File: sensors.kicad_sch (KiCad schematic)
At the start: 15 parts, among them U21 BMI088 6-axis IMU, U22 BMP581 barometer, U23 ADXL375 high-g accelerometer

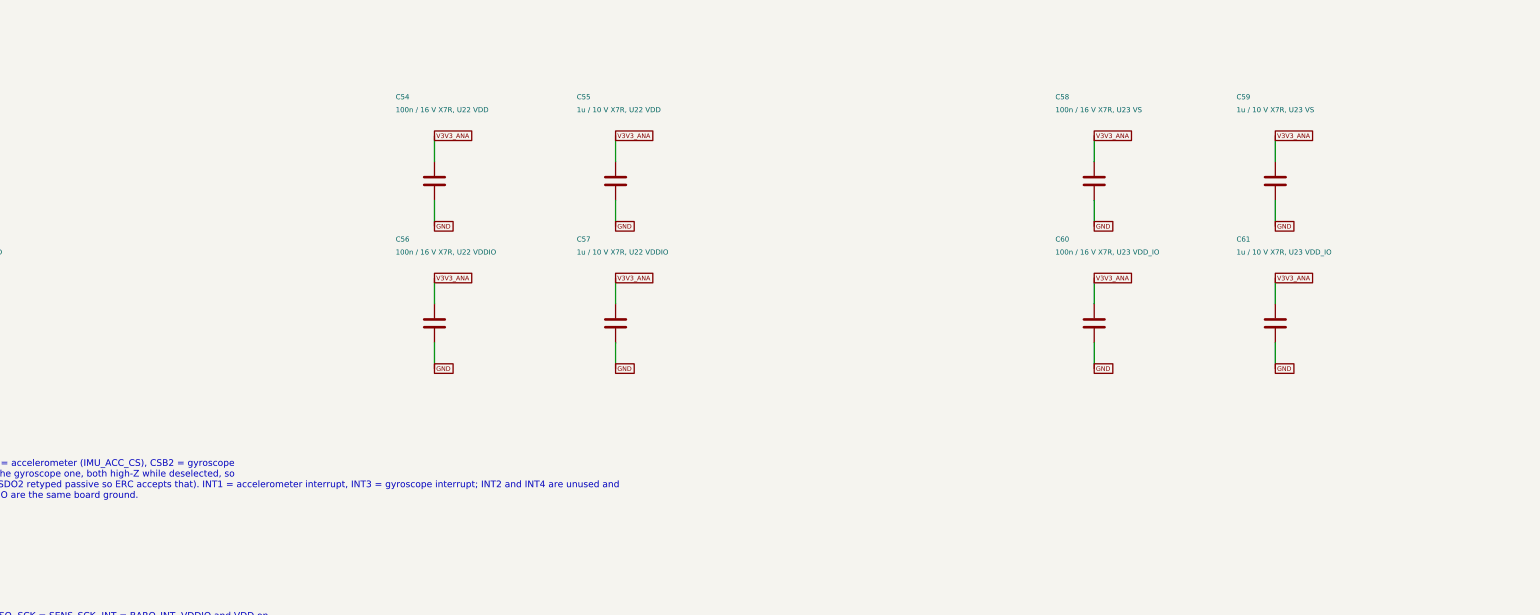
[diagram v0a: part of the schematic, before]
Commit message: Schematic review: TPS2121 input stage, DS-009 ports, sequencing and CS fixes; docs trimmed
Datasheet-grounded review of the full flight-controller schematic. Downstream
of the input everything verified pin-by-pin (TPS62913, TPS7A20, RP2354B,
BMI088/BMP581/ADXL375, W25Q128, microSD, PWM). The 5 V input stage did not:

- LM66100 (5.5 V rec-op / 6 V abs-max) replaced by one TPS2121 mux (U25):
  BEC priority on IN1, OV lockout ~5.86 V, current limit ~1.5 A, reverse
  blocking on both inputs, source status on GPIO39. Input spec 4.75-5.5 V.
- 5V_IN: 2x4.7 uF + 100 uF + SMAJ5.0A TVS; J3 JST-XH -> XT30PW-M (pin 1 GND).
- J6/J7/J9 reordered to Pixhawk DS-009 (VCC/sig/sig/GND); GPS/ELRS VCC 5 V.
- VIN_SENSE 22k/10k (full scale 10.6 V, was saturating at 5.5 V).
- TPS7A20 EN <- PWR_GOOD so V3V3_ANA rises after V3V3_SYS.
- RP2354B VREG_AVDD moved to V3V3_SYS (datasheet 6.1.8: must power up with
  VREG_VIN); ADC_AVDD stays on V3V3_ANA.
- 10k pull-ups on the four sensor chip-selects.
- ERC "global label appears once" re-enabled (0 hits).

Generator, netlist checker and SPICE decks updated (TPS2121 behavioral model,
new over-voltage and 2S mis-plug corners). Build idempotent, 143 pin mappings
PASS, ERC 0/0, all corners PASS.

Docs: POWER_*.md history removed, rationale folded into DESIGN_SPEC Decisions;
808 -> 290 lines across README, DESIGN_SPEC, LIBRARIES, simulations/README.

Co-Authored-By: Claude Fable 5.1 <noreply@anthropic.com>
Claude-Session: https://claude.ai/code/session_015cFNiWgf35VN2T43HaK8PE
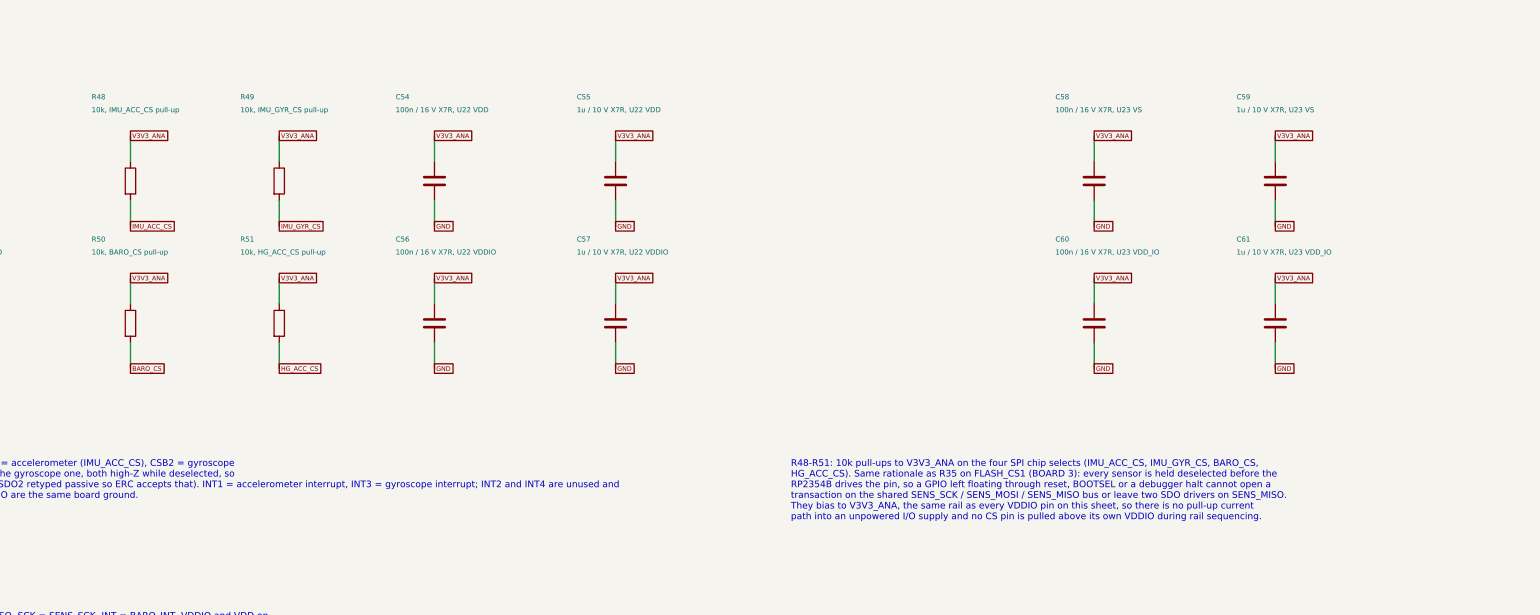
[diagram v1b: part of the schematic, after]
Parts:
- added R48: 10k, IMU_ACC_CS pull-up, Resistor_SMD:R_0603_1608Metric, symbol Device:R
- added R49: 10k, IMU_GYR_CS pull-up, Resistor_SMD:R_0603_1608Metric, symbol Device:R
- added R50: 10k, BARO_CS pull-up, Resistor_SMD:R_0603_1608Metric, symbol Device:R
- added R51: 10k, HG_ACC_CS pull-up, Resistor_SMD:R_0603_1608Metric, symbol Device:R
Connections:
- net BARO_CS: now also R50.2
- net HG_ACC_CS: now also R51.2
- net IMU_ACC_CS: now also R48.2
- net IMU_GYR_CS: now also R49.2
- net V3V3_ANA: now also R48.1, R49.1, R50.1, R51.1
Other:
- note added: "R48-R51: 10k pull-ups to V3V3_ANA on the four SPI chip selects (IMU_ACC_CS, IMU_GYR_CS, BARO_CS, HG_ACC_CS). Same rationale as R35 on FLASH_CS1 (BOARD 3): every sensor is held deselected before the RP2354B drives the pin, so a GPIO left floating through reset, BOOTSEL or a debugger halt cannot open a transaction on the shared SENS_SCK / SENS_MOSI / SENS_MISO bus or leave two SDO drivers on SENS_M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"

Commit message: Replace BMI088 with ICM-45686; vendor all footprints and 3D models for layout
Sensors: U21 is now the TDK ICM-45686 (single AP_CS on GPIO20 as IMU_CS,
INT1/INT2 on GPIO23/24, GPIO21 spare, R49 dropped, VDD+VDDIO on V3V3_ANA
with 100 nF + 1 uF each). Project-local symbol, footprint and stand-in STEP;
footprint numbering verified against DS-000577 Rev 1.0 Sec 11.2 (CCW, top
view). BMI088_SPI derived-symbol machinery removed from the generator.

Layout readiness: new tools/audit_footprints.py checks every component for
a resolvable footprint and present 3D model (128/128 OK). The seven official
KiCad footprints whose STEP files are absent from kicad-packages3d 10.0.6
are vendored into MARV_Packages.pretty with project-local models in
MARV_Packages.3dshapes: manufacturer STEPs (Coilcraft XGL4030, Molex
104031-0811), EasyEDA model (HRO TYPE-C-31-M-12), FreeCAD-generated bodies
from tools/3d/ (RP2354B QFN-80, TPS62913 RPU0010A, TPS2121 RUX0012A, Amass
XT30PW-M), and KiCad generic stand-ins (BMP581, ADXL375). Model offsets were
derived by measurement and confirmed in a rendered check board.
PROVENANCE.md records source, licence and SHA256 per model; LIBRARIES.md
lists the pre-fab 3D-viewer checks and the unverified dimensions.

Checks: build idempotent, ERC 0/0, check_power_netlist 149 mappings /
128 components, run_power_checks PASS, audit 0 needing action.

Co-Authored-By: Claude Fable 5.1 <noreply@anthropic.com>
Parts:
- removed R49: 10k, IMU_GYR_CS pull-up, Resistor_SMD:R_0603_1608Metric, symbol Device:R
- R48: value 10k, IMU_ACC_CS pull-up -> 10k, IMU_CS pull-up
- U21: value BMI088 6-axis IMU -> ICM-45686 6-axis IMU; footprint Package_LGA:Bosch_LGA-16_4.5x3mm_P0.5mm_LayoutBorder7x1y_ClockwisePinNumbering -> MARV_Packages:InvenSense_LGA-14_2.5x3mm_P0.5mm_ICM45686; symbol MARV_Power:BMI088_SPI -> MARV_Sensors:ICM-45686
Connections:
- net IMU_GYR_CS is gone; now on net V3V3_ANA: U21.5 (VDDIO)
- net IMU_GYR_INT is gone; now on net IMU_CS: U21.12 (AP_CS)
- net GND: no longer U21.2 (GNDA), U21.4 (GNDA), U21.7 (PS)
- net SENS_MISO: now also U21.1 (AP_SDO); no longer U21.10 (SDO2), U21.15 (SDO1)
- net SENS_MOSI: now also U21.14 (AP_SDA/AP_SDIO/AP_SDI); no longer U21.9 (SDI/SDA)
- net SENS_SCK: now also U21.13 (AP_SCLK); no longer U21.8 (SCK/SCL)
- net V3V3_ANA: now also U21.8 (VDD); no longer U21.11 (VDDIO), U21.3 (VDD)
- net IMU_ACC_CS renamed IMU_CS
- net IMU_CS: no longer U21.14 (~{CSB1})
- removed net IMU_ACC_INT: U21.16 (INT1)
- new net IMU_INT1: U21.4 (INT1)
- new net IMU_INT2: U21.9 (INT2/FSYNC/CLKIN)
- no-connect marks 4 -> 7
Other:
- note added: "All three sensors run 4-wire SPI on the shared SENS_SCK / SENS_MOSI / SENS_MISO bus with one chip select each, and are powered from V3V3_ANA (TPS7A20 LDO). Every supply pin on this sheet gets 100 nF + 1 uF: BMP581 and ADXL375 because their own datasheets call for the pair, the ICM-45686 as a deliberate addition - its datasheet BOM (DS-000577 Rev 1.0 Table 11) lists 0.1 uF only."
- note added: "R48, R50, R51: 10k pull-ups to V3V3_ANA on the three SPI chip selects (IMU_CS, BARO_CS, HG_ACC_CS). R49 (the former second IMU chip-select pull-up) is removed along with that net - the ICM-45686 has a single chip select. Same rationale as R35 on FLASH_CS1 (BOARD 3): every sensor is held deselected before the RP2354B drives the pin, so a GPIO left floating through reset, BOOTSEL or a debugger halt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"
- note added: "U21 ICM-45686 (TDK InvenSense DS-000577 Rev 1.0, Table 10 "Signal Descriptions" / Figure 4 pin-out, Single Interface SPI mode, Figure 10): AP_CS (pin 12) = IMU_CS, AP_SCLK (13) = SENS_SCK, AP_SDA/AP_SDIO/AP_SDI (14) = SENS_MOSI, AP_SDO/AP_AD0 (1) = SENS_MISO. INT1 (4) = IMU_INT1. INT2/FSYNC/CLKIN (9) = IMU_INT2 - typed bidirectional because FSYNC/CLKIN are host-driven inputs while INT2 is a chip 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"
- note removed: "All three sensors run 4-wire SPI on the shared SENS_SCK / SENS_MOSI / SENS_MISO bus with one chip select each, and are powered from V3V3_ANA (TPS7A20 LDO) with 100 nF + 1 uF at every supply pin per datasheet."
- note removed: "R48-R51: 10k pull-ups to V3V3_ANA on the four SPI chip selects (IMU_ACC_CS, IMU_GYR_CS, BARO_CS, HG_ACC_CS). Same rationale as R35 on FLASH_CS1 (BOARD 3): every sensor is held deselected before the RP2354B drives the pin, so a GPIO left floating through reset, BOOTSEL or a debugger halt cannot open a transaction on the shared SENS_SCK / SENS_MOSI / SENS_MISO bus or leave two SDO drivers on SENS_M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"
- note removed: "U21 BMI088 (datasheet Sec 6.2): PS tied to GND selects SPI. CSB1 = accelerometer (IMU_ACC_CS), CSB2 = gyroscope (IMU_GYR_CS); SDO1 is the accelerometer data output and SDO2 the gyroscope one, both high-Z while deselected, so they share SENS_MISO (the symbol is Sensor_Motion:BMI088 with SDO2 retyped passive so ERC accepts that). INT1 = accelerometer interrupt, INT3 = gyroscope interrupt; INT2 and 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"

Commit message: Physical design: VBAT-in buck, ESC pad row, pad-row IO, 50 mm single-sided board
Power: the FC now takes raw 2-6S VBAT from the MicoAir AM32 4-in-1 ESC pad
row (CURR TX M4 M3 M2 M1 VBAT GND, J3) through an AP63205WU 5 V/2 A buck
(U26, XGL4030-472, 3 x 22 uF) into the existing TPS2121 mux; XT30 and its
TVS removed. VBAT sense 100k/10k (36 V FS) on ADC0, ESC current sense on
ADC2, ESC KISS telemetry on GPIO30.

IO per the physical spec (DESIGN_SPEC "Physical design"): solder pad rows
for GPS/ELRS/MAG (JST-GH removed), DBG and buzzer; 3x4 servo block for
PWM5-8; 2x6 spare-IO block; WS2812C-2020 RGB LED replaces the two discrete
LEDs; buzzer moved off-board to pads; flash socket is the 150-mil SOIC-8
(W25Q64 default, APS6404L PSRAM alternative); four 4.0 mm grommet holes on
the 30.5 mm pattern. Passives moved to 0402/0603 for the single-sided
envelope.

Board: tools/setup_pcb.py regenerates MARV-V2.kicad_pcb from the netlist —
50 x 50 mm, 4-layer JLC 7628 stack-up, net classes incl. a 90 ohm USB pair,
edge-anchored connectors, coarse interior placement, silk pad labels.
DRC leaves only unrouted items. The BMP581 project footprint had its 2-pad
edges at +/-0.5 mm (corner pads overlapped, three nets shorted); corrected
to Bosch Fig. 32 (+/-0.25 mm, 0.20 mm gaps).

Checks: ERC 0/0, 217 pin mappings / 139 components, run_power_checks PASS,
audit 139/139, pcb DRC unrouted-only.

Co-Authored-By: Claude Fable 5.1 <noreply@anthropic.com>
Claude-Session: https://claude.ai/code/session_01U6Ud7JA3CDTJZVcZZr5sx1
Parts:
- C50, C52, C54, C56, C58, C60: footprint Capacitor_SMD:C_0805_2012Metric -> Capacitor_SMD:C_0402_1005Metric
- C51: value 1u / 10 V X7R, U21 VDD -> 1u / 10 V X7R 0603, U21 VDD; footprint Capacitor_SMD:C_0805_2012Metric -> Capacitor_SMD:C_0603_1608Metric
- C53: value 1u / 10 V X7R, U21 VDDIO -> 1u / 10 V X7R 0603, U21 VDDIO; footprint Capacitor_SMD:C_0805_2012Metric -> Capacitor_SMD:C_0603_1608Metric
- C55: value 1u / 10 V X7R, U22 VDD -> 1u / 10 V X7R 0603, U22 VDD; footprint Capacitor_SMD:C_0805_2012Metric -> Capacitor_SMD:C_0603_1608Metric
- C57: value 1u / 10 V X7R, U22 VDDIO -> 1u / 10 V X7R 0603, U22 VDDIO; footprint Capacitor_SMD:C_0805_2012Metric -> Capacitor_SMD:C_0603_1608Metric
- C59: value 1u / 10 V X7R, U23 VS -> 1u / 10 V X7R 0603, U23 VS; footprint Capacitor_SMD:C_0805_2012Metric -> Capacitor_SMD:C_0603_1608Metric
- C61: value 1u / 10 V X7R, U23 VDD_IO -> 1u / 10 V X7R 0603, U23 VDD_IO; footprint Capacitor_SMD:C_0805_2012Metric -> Capacitor_SMD:C_0603_1608Metric
- R48, R50, R51: footprint Resistor_SMD:R_0603_1608Metric -> Resistor_SMD:R_0402_1005Metric

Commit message: Remove buzzer; passives to 0201/0402; GPIO28 to spare-IO block
Buzzer pads J15, driver Q20/D22/R33/R34 and the BUZZ nets removed; GPIO28
now terminates on J16 pin 12 (was a second GND). Resistors 0201, caps
<= 4.7 uF 0402, 22 uF/10 V 0603, 22 uF/25 V and 10 uF/50 V 0805, 47 uF
0805; USB net-class clearance 0.18 mm so the 0201 series resistors on the
pair pass DRC. Board regenerated at 50 x 50 mm (courtyard fill 63.5 %);
DRC unrouted-only. 134 components, 105 nets; ERC 0/0, 213 pin mappings,
run_power_checks PASS, audit 134/134.

Co-Authored-By: Claude Fable 5.1 <noreply@anthropic.com>
Claude-Session: https://claude.ai/code/session_01U6Ud7JA3CDTJZVcZZr5sx1
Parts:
- C51: value 1u / 10 V X7R 0603, U21 VDD -> 1u / 10 V X7R 0402, U21 VDD; footprint Capacitor_SMD:C_0603_1608Metric -> Capacitor_SMD:C_0402_1005Metric
- C53: value 1u / 10 V X7R 0603, U21 VDDIO -> 1u / 10 V X7R 0402, U21 VDDIO; footprint Capacitor_SMD:C_0603_1608Metric -> Capacitor_SMD:C_0402_1005Metric
- C55: value 1u / 10 V X7R 0603, U22 VDD -> 1u / 10 V X7R 0402, U22 VDD; footprint Capacitor_SMD:C_0603_1608Metric -> Capacitor_SMD:C_0402_1005Metric
- C57: value 1u / 10 V X7R 0603, U22 VDDIO -> 1u / 10 V X7R 0402, U22 VDDIO; footprint Capacitor_SMD:C_0603_1608Metric -> Capacitor_SMD:C_0402_1005Metric
- C59: value 1u / 10 V X7R 0603, U23 VS -> 1u / 10 V X7R 0402, U23 VS; footprint Capacitor_SMD:C_0603_1608Metric -> Capacitor_SMD:C_0402_1005Metric
- C61: value 1u / 10 V X7R 0603, U23 VDD_IO -> 1u / 10 V X7R 0402, U23 VDD_IO; footprint Capacitor_SMD:C_0603_1608Metric -> Capacitor_SMD:C_0402_1005Metric
- R48, R50, R51: footprint Resistor_SMD:R_0402_1005Metric -> Resistor_SMD:R_0201_0603Metric

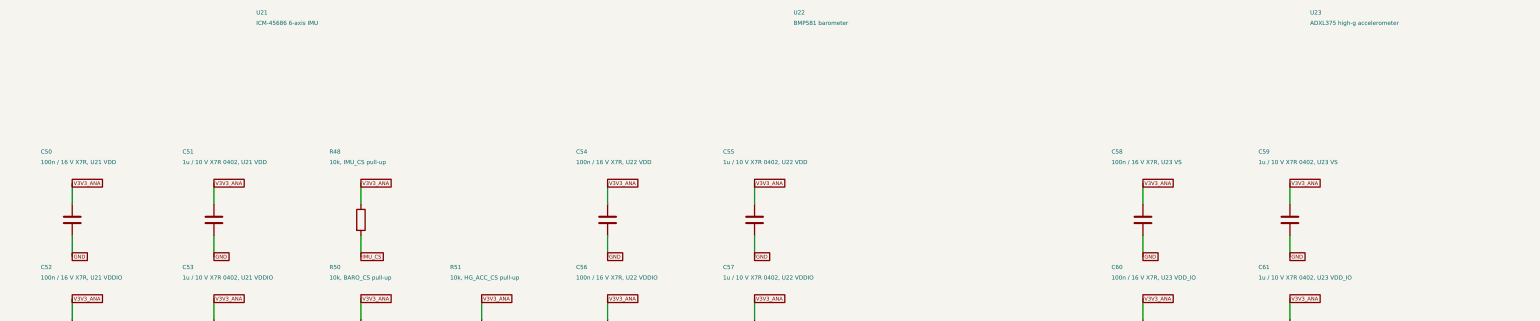
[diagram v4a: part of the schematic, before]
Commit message: IO array replaces bus pad rows; PINOUT.md pin plan; test points; ESC/battery docs
Left edge is now one 2 x 16 through-hole IO array (J6, signal | 5V/3V3/GND
rows, madflight-style) carrying GPS/ELRS/MAG and the ten spare GPIOs; the
J6/J7/J9 pad rows and the J16 block are gone. ESC pad row J3 and DBG pads
J10 stay; servo block J12-J14 stays beside the ESC row. TP1-TP10 1 mm test
points on the sensor SPI, chip selects and interrupts.

PINOUT.md records every GPIO's function and alternates from RP2350
datasheet Table 3, the spare-pin roles (I2C0 on 44/45, SPI1 on 46/47/28,
ADC3-7) and the peripheral ledger; check_power_netlist.py now asserts all
48 GPIO nets against it.

DESIGN_SPEC: ESC connection table, IO array table, test points, battery
monitoring (VBAT_SENSE + ESC current; INA226 rejected), edge allocation.
setup_pcb.py vendors the header footprints with project-local 3D models;
board 50 x 50 mm (48 collides with the grommet keepouts), DRC unrouted-only.
141 components, 105 nets, 231 pin mappings; ERC 0/0, ngspice PASS,
audit 141/141.

Co-Authored-By: Claude Fable 5.1 <noreply@anthropic.com>
Claude-Session: https://claude.ai/code/session_01U6Ud7JA3CDTJZVcZZr5sx1
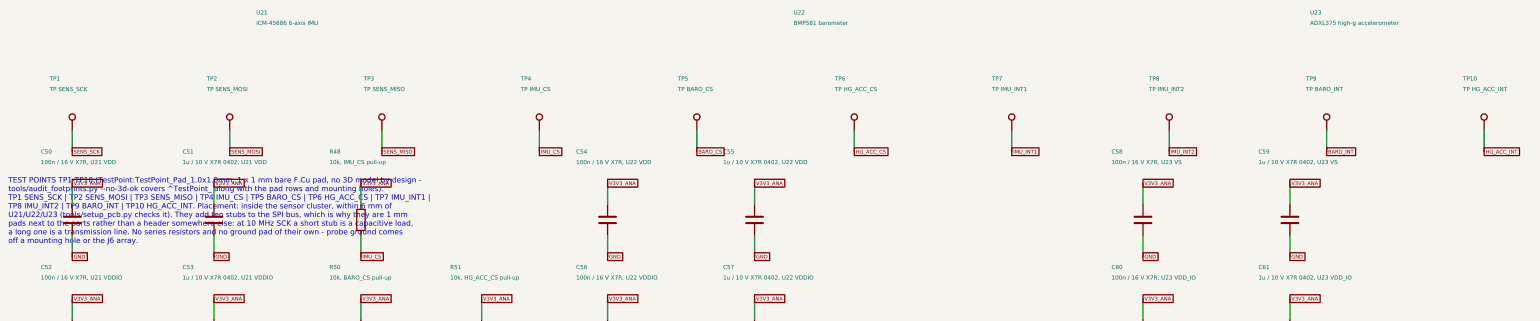
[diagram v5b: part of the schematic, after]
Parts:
- added TP1: TP SENS_SCK, TestPoint:TestPoint_Pad_1.0x1.0mm, symbol Connector:TestPoint
- added TP10: TP HG_ACC_INT, TestPoint:TestPoint_Pad_1.0x1.0mm, symbol Connector:TestPoint
- added TP2: TP SENS_MOSI, TestPoint:TestPoint_Pad_1.0x1.0mm, symbol Connector:TestPoint
- added TP3: TP SENS_MISO, TestPoint:TestPoint_Pad_1.0x1.0mm, symbol Connector:TestPoint
- added TP4: TP IMU_CS, TestPoint:TestPoint_Pad_1.0x1.0mm, symbol Connector:TestPoint
- added TP5: TP BARO_CS, TestPoint:TestPoint_Pad_1.0x1.0mm, symbol Connector:TestPoint
- added TP6: TP HG_ACC_CS, TestPoint:TestPoint_Pad_1.0x1.0mm, symbol Connector:TestPoint
- added TP7: TP IMU_INT1, TestPoint:TestPoint_Pad_1.0x1.0mm, symbol Connector:TestPoint
- added TP8: TP IMU_INT2, TestPoint:TestPoint_Pad_1.0x1.0mm, symbol Connector:TestPoint
- added TP9: TP BARO_INT, TestPoint:TestPoint_Pad_1.0x1.0mm, symbol Connector:TestPoint
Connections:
- net BARO_CS: now also TP5.1
- net BARO_INT: now also TP9.1
- net HG_ACC_CS: now also TP6.1
- net HG_ACC_INT: now also TP10.1
- net IMU_CS: now also TP4.1
- net IMU_INT1: now also TP7.1
- net IMU_INT2: now also TP8.1
- net SENS_MISO: now also TP3.1
- net SENS_MOSI: now also TP2.1
- net SENS_SCK: now also TP1.1
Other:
- note added: "TEST POINTS TP1-TP10 (TestPoint:TestPoint_Pad_1.0x1.0mm, 1 x 1 mm bare F.Cu pad, no 3D model by design - tools/audit_footprints.py --no-3d-ok covers ^TestPoint_ along with the pad rows and mounting holes). TP1 SENS_SCK | TP2 SENS_MOSI | TP3 SENS_MISO | TP4 IMU_CS | TP5 BARO_CS | TP6 HG_ACC_CS | TP7 IMU_INT1 | TP8 IMU_INT2 | TP9 BARO_INT | TP10 HG_ACC_INT. Placement: inside the sensor cluster, wit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"

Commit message: JLCPCB sourcing: Basic-part refactor, LCSC numbers in the schematic, order files and audit
Parts audited line by line against JLCPCB's live catalogue (tools/jlc/,
reports/jlc-audit.md). Resistors move 0201 -> 0402 (JLC's Basic library has
no 0201 resistor), the U7 FB divider becomes 10k/3.16k 0.1 % (15.8k 0.1 % is
not stocked), Y1 becomes TAXM12M4RFBCCT2T (CL 12 pF) with 18 pF loads, L2/L3
become CJIANG FTC303020D2R2MBCA / FTC404030S4R7MGCA (stocked; Isat 5.5 A /
6.0 A at 30 %, footprints + models vendored from KiCad), the 22 uF/25 V and
10 uF lines move to Basic parts. The U24 default fit is W25Q32JVSNIQ (the
W25Q64JVSSIQ is a 208-mil part and never fitted the 150-mil socket).

Every fitted symbol carries a hidden LCSC property stamped from
tools/jlc/lcsc_map.csv; tools/jlc/export_jlc.py writes reports/jlc-bom.csv
and reports/jlc-cpl.csv (top-side SMT, headers unpopulated, U24 DNP).
Result: 46 unique parts, 16 Basic / 1 Preferred / 29 Extended (was 9/1/35),
extended-fee estimate $87 (was $105), $45.68 per board at 10 (was $52.97 with
L2 unsourced). DESIGN_SPEC gains a Manufacturing (JLCPCB) section with the
quote parameters. Board rebuilt (0 fit/geometry, DRC unrouted-only); ERC
0/0, checker PASS, ngspice PASS, audit 140/140.

Co-Authored-By: Claude Fable 5.1 <noreply@anthropic.com>
Claude-Session: https://claude.ai/code/session_01U6Ud7JA3CDTJZVcZZr5sx1
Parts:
- C50, C52, C54, C56, C58, C60: LCSC (none) -> C1525
- C51, C53, C55, C57, C59, C61: LCSC (none) -> C52923
- R48, R50, R51: footprint Resistor_SMD:R_0201_0603Metric -> Resistor_SMD:R_0402_1005Metric; LCSC (none) -> C25744
- U21: LCSC (none) -> C22459454
- U22: LCSC (none) -> C5362283
- U23: LCSC (none) -> C579466
